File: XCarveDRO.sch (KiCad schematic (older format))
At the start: 9 parts, among them J103 USB_A, Q1 IRLML0040TR, SW103 SEL1, SW104 SEL2, U101 Teensy4.1

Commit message: Based on feedback, update silkscreen on DP101 and link to OSHPark, R201 from 10K to 1K.
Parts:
- J103: symbol Connector:USB_A -> XCarveDRO-rescue:USB_A-Connector
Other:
- note added: "DP101 Can be ordered from OshPark:\nhttps://oshpark.com/shared_projects/ZNeN5t92\nThis breakout includes R101 and Q1 so they\ncan be ignored in this schematic."
- note removed: "DP101 Can be ordered from OshPark:\nhttps://oshpark.com/shared_projects/djFs49lT"
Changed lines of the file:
@@
 	3950 850  8100 850
 $Comp
-L Connector:USB_A J103
+L XCarveDRO-rescue:USB_A-Connector J103
 U 1 1 5FADCB7A
 P 3800 5800
@@
 Wire Notes Line
 	11100 5350 6950 5350
-Text Notes 700  900  0    79   ~ 0
-DP101 Can be ordered from OshPark:\nhttps://oshpark.com/shared_projects/djFs49lT
+Text Notes 650  1100 0    79   ~ 0
+DP101 Can be ordered from OshPark:\nhttps://oshpark.com/shared_projects/ZNeN5t92\nThis breakout includes R101 and Q1 so they\ncan be ignored in this schematic.
 Wire Notes Line
-	650  600  650  1000
+	650  1100 3600 1100
 Wire Notes Line
-	650  1000 3600 1000
+	3600 600  3600 1100
 Wire Notes Line
-	3600 1000 3600 600
+	650  600  650  1100
 Wire Notes Line
-	3600 600  650  600
+	650  600  3600 600
 $EndSCHEMATC

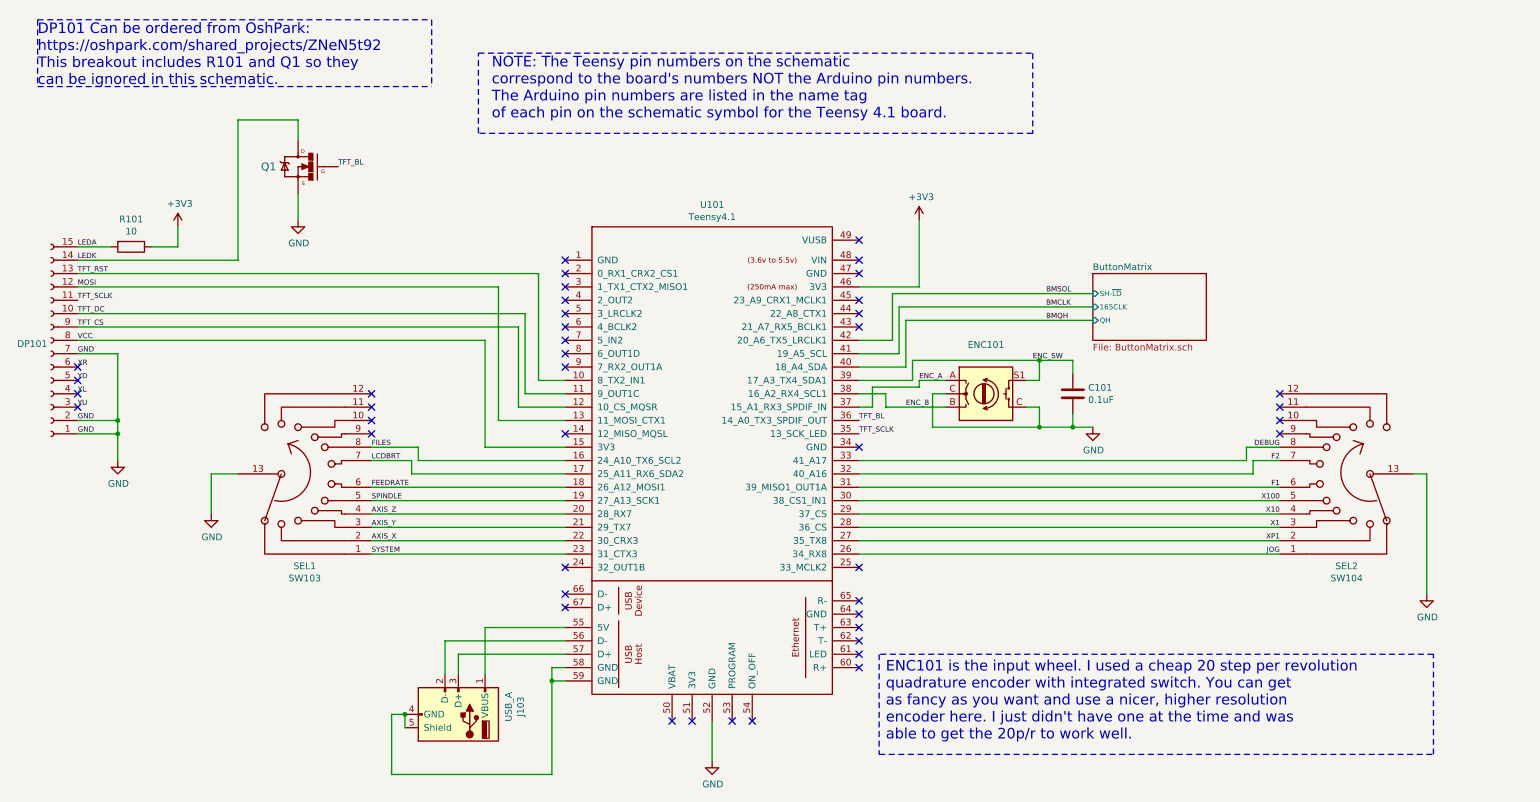
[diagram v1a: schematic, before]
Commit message: Update schematic to use the oshpark board layout so there is more consistency between the two. Update notes descriptions and bump to revision 1.
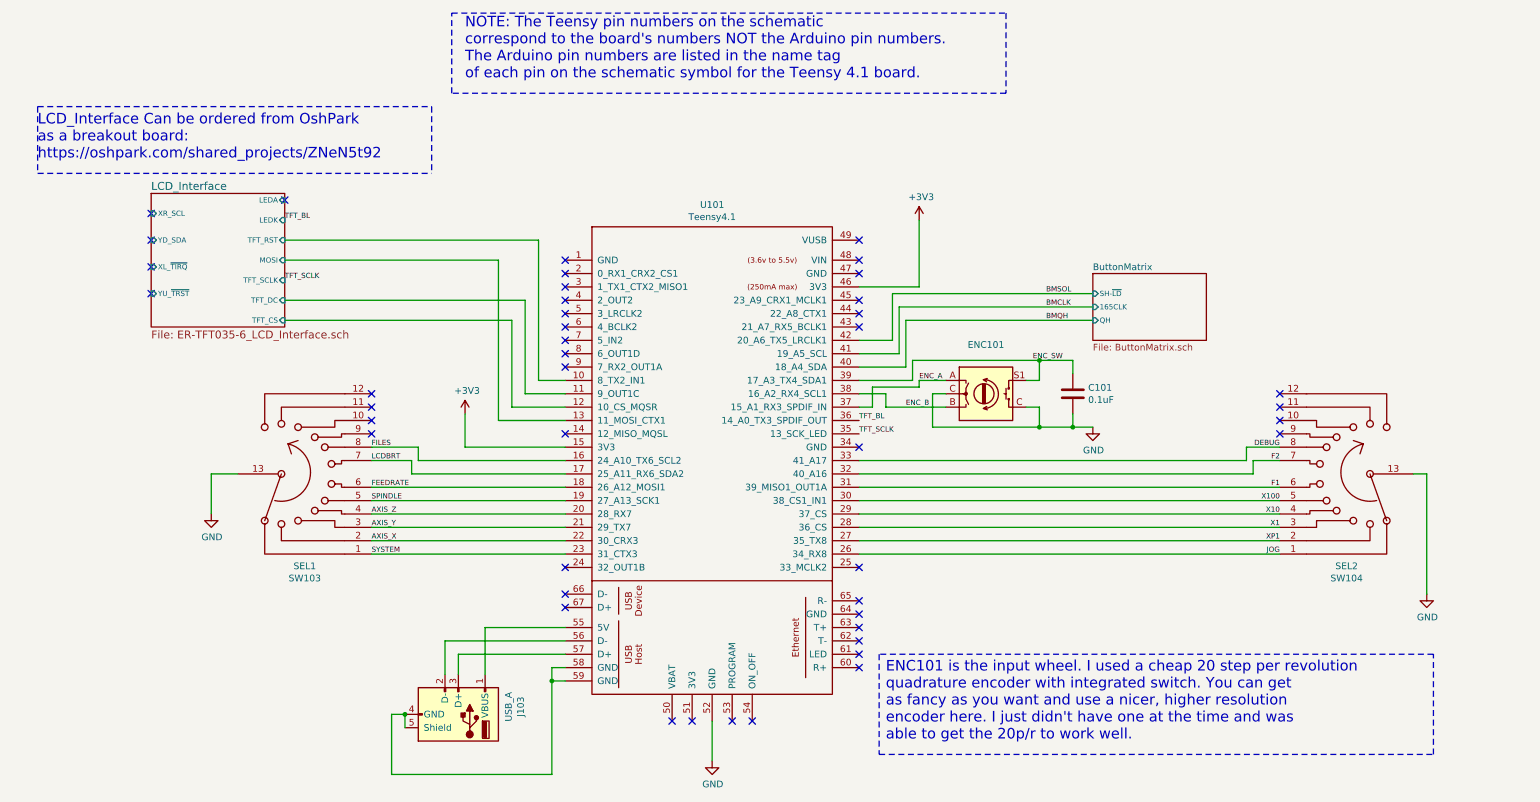
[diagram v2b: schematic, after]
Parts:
- removed DP101: Conn_01x15_Female, MarcoK:BUY_LCD_TFT035-6_320x480-BO, symbol Connector:Conn_01x15_Female
- removed Q1: IRLML0040TR, symbol MarcoK:IRLML0040TR
- removed R101: 10, symbol Device:R
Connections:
- net VCC is gone; now on net +3V3: U101.15 (3V3)
- net MOSI renamed LCD_Interface/MOSI
- net TFT_CS renamed LCD_Interface/TFT_CS
- net TFT_DC renamed LCD_Interface/TFT_DC
- net TFT_RST renamed LCD_Interface/TFT_RST
- no-connect marks 43 -> 44
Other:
- note added: "LCD_Interface Can be ordered from OshPark\nas a breakout board:\nhttps://oshpark.com/shared_projects/ZNeN5t92"
- note removed: "DP101 Can be ordered from OshPark:\nhttps://oshpark.com/shared_projects/ZNeN5t92\nThis breakout includes R101 and Q1 so they\ncan be ignored in this schematic."
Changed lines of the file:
@@
 $Descr A4 11693 8268
 encoding utf-8
-Sheet 1 2
+Sheet 1 3
 Title "GRBL Controller"
-Date "2021-01-09"
-Rev "0"
+Date "2022-01-10"
+Rev "1"
 Comp ""
-Comment1 "DP101 is a TFT LCD breakout adapter for the ER-TFT035-6 from BuyDisplay.com"
+Comment1 "MCU, encoder and selector switches."
 Comment2 ""
 Comment3 ""
@@
 	1    7750 3400
 	1    0    0    -1
-$EndComp
-Text Label 950  3600 0    39   ~ 0
-GND
-Text Label 950  3700 0    39   ~ 0
-GND
-Text Label 950  3100 0    39   ~ 0
-GND
-Text Label 950  2800 0    39   ~ 0
-TFT_DC
-Text Label 950  2600 0    39   ~ 0
-MOSI
-Text Label 950  2700 0    39   ~ 0
-TFT_SCLK
-Text Label 950  2900 0    39   ~ 0
-TFT_CS
-Text Label 950  2400 0    39   ~ 0
-LEDK
-Text Label 950  2300 0    39   ~ 0
-LEDA
-Text Label 950  3300 0    39   ~ 0
-YD
-Text Label 950  3500 0    39   ~ 0
-YU
-Text Label 950  3200 0    39   ~ 0
-XR
-Text Label 950  3400 0    39   ~ 0
-XL
-Text Label 950  2500 0    39   ~ 0
-TFT_RST
-Text Label 950  3000 0    39   ~ 0
-VCC
-$Comp
-L Connector:Conn_01x15_Female J?
-U 1 1 5FBD7E6A
-P 750 3000
-AR Path="/5FBAC065/5FBD7E6A" Ref="J?"  Part="1"
-AR Path="/5FBD7E6A" Ref="DP101"  Part="1"
-F 0 "DP101" H 778 3026 50  0000 L CNN
-F 1 "Conn_01x15_Female" H 778 2935 50  0001 L CNN
-F 2 "MarcoK:BUY_LCD_TFT035-6_320x480-BO" H 750 3000 50  0001 C CNN
-F 3 "~" H 750 3000 50  0001 C CNN
-F 4 "https://oshpark.com/shared_projects/djFs49lT" H 750 3000 50  0001 C CNN "OshPArk"
-	1    750  3000
-	-1   0    0    1
 $EndComp
 $Sheet
@@
 NoConn ~ 4600 2400
 NoConn ~ 5550 5850
-$Comp
-L power:GND #PWR0105
-U 1 1 60629CFA
-P 1250 3900
-F 0 "#PWR0105" H 1250 3650 50  0001 C CNN
-F 1 "GND" H 1255 3727 50  0000 C CNN
-F 2 "" H 1250 3900 50  0001 C CNN
-F 3 "" H 1250 3900 50  0001 C CNN
-	1    1250 3900
-	1    0    0    -1
-$EndComp
-$Comp
-L MarcoK:IRLML0040TR Q1
-U 1 1 6062DC4C
-P 2600 1700
-F 0 "Q1" H 2763 1700 59  0000 L CNN
-F 1 "IRLML0040TR" H 2763 1648 59  0001 L CNN
-F 2 "" H 2600 1700 10  0001 C CNN
-F 3 "" H 2600 1700 10  0001 C CNN
-	1    2600 1700
-	-1   0    0    -1
-$EndComp
-$Comp
-L power:GND #PWR0106
-U 1 1 6063E03D
-P 2600 2100
-F 0 "#PWR0106" H 2600 1850 50  0001 C CNN
-F 1 "GND" H 2605 1927 50  0000 C CNN
-F 2 "" H 2600 2100 50  0001 C CNN
-F 3 "" H 2600 2100 50  0001 C CNN
-	1    2600 2100
-	1    0    0    -1
-$EndComp
-$Comp
-L Device:R R101
-U 1 1 6063E605
-P 1350 2300
-F 0 "R101" V 1143 2300 50  0000 C CNN
-F 1 "10" V 1234 2300 50  0000 C CNN
-F 2 "" V 1280 2300 50  0001 C CNN
-F 3 "~" H 1350 2300 50  0001 C CNN
-	1    1350 2300
-	0    1    1    0
-$EndComp
-Wire Wire Line
-	950  2300 1200 2300
-Text Label 2900 1700 0    39   ~ 0
-TFT_BL
-Wire Wire Line
-	950  3700 1250 3700
-Wire Wire Line
-	1250 3700 1250 3900
-Wire Wire Line
-	950  3600 1250 3600
-Wire Wire Line
-	1250 3600 1250 3700
-Connection ~ 1250 3700
-NoConn ~ 950  3500
-NoConn ~ 950  3400
-NoConn ~ 950  3300
-NoConn ~ 950  3200
-Wire Wire Line
-	950  3100 1250 3100
-Wire Wire Line
-	1250 3100 1250 3600
-Connection ~ 1250 3600
-Wire Wire Line
-	950  2500 4400 2500
-Wire Wire Line
-	4400 2500 4400 3300
 Wire Wire Line
 	4400 3300 4600 3300
 Wire Wire Line
 	4600 3400 4300 3400
-Wire Wire Line
-	4300 3400 4300 2800
-Wire Wire Line
-	4300 2800 950  2800
-Wire Wire Line
-	4600 3500 4250 3500
-Wire Wire Line
-	4250 3500 4250 2900
-Wire Wire Line
-	4250 2900 950  2900
-Wire Wire Line
-	4100 2600 4100 3600
 Wire Wire Line
 	4100 3600 4600 3600
@@
 L power:+3V3 #PWR0107
 U 1 1 606A3138
-P 7250 2100
-F 0 "#PWR0107" H 7250 1950 50  0001 C CNN
-F 1 "+3V3" H 7265 2273 50  0000 C CNN
-F 2 "" H 7250 2100 50  0001 C CNN
-F 3 "" H 7250 2100 50  0001 C CNN
-	1    7250 2100
+P 3850 3550
+F 0 "#PWR0107" H 3850 3400 50  0001 C CNN
+F 1 "+3V3" H 3865 3723 50  0000 C CNN
+F 2 "" H 3850 3550 50  0001 C CNN
+F 3 "" H 3850 3550 50  0001 C CNN
+	1    3850 3550
 	1    0    0    -1
 $EndComp
@@
 	7250 2600 7250 2100
 NoConn ~ 6800 2500
-$Comp
-L power:+3V3 #PWR0108
-U 1 1 606AB99C
-P 1700 2150
-F 0 "#PWR0108" H 1700 2000 50  0001 C CNN
-F 1 "+3V3" H 1715 2323 50  0000 C CNN
-F 2 "" H 1700 2150 50  0001 C CNN
-F 3 "" H 1700 2150 50  0001 C CNN
-	1    1700 2150
-	1    0    0    -1
-$EndComp
-Wire Wire Line
-	1500 2300 1700 2300
-Wire Wire Line
-	1700 2300 1700 2150
-Wire Wire Line
-	4000 3800 4000 3000
-Wire Wire Line
-	4000 3000 950  3000
-Wire Wire Line
-	4000 3800 4600 3800
-Wire Wire Line
-	950  2600 4100 2600
-Wire Wire Line
-	2600 2100 2600 1900
-Wire Wire Line
-	950  2400 2150 2400
-Wire Wire Line
-	2150 2400 2150 1350
-Wire Wire Line
-	2150 1350 2600 1350
-Wire Wire Line
-	2600 1350 2600 1500
 Text Label 7250 3300 0    39   ~ 0
 ENC_A
@@
 Text Label 8200 2850 0    39   ~ 0
 BMQH
-Text Notes 4050 1350 0    79   ~ 0
+Text Notes 3850 1050 0    79   ~ 0
 NOTE: The Teensy pin numbers on the schematic\ncorrespond to the board's numbers NOT the Arduino pin numbers.\nThe Arduino pin numbers are listed in the name tag\nof each pin on the schematic symbol for the Teensy 4.1 board.
 Wire Notes Line
-	8100 850  8100 1450
-Wire Notes Line
-	8100 1450 3950 1450
-Wire Notes Line
-	3950 1450 3950 850
-Wire Notes Line
-	3950 850  8100 850
+	7900 550  7900 1150
+Wire Notes Line
+	7900 1150 3750 1150
+Wire Notes Line
+	3750 1150 3750 550
+Wire Notes Line
+	3750 550  7900 550
 $Comp
 L XCarveDRO-rescue:USB_A-Connector J103
@@
 Wire Notes Line
 	11100 5350 6950 5350
-Text Notes 650  1100 0    79   ~ 0
-DP101 Can be ordered from OshPark:\nhttps://oshpark.com/shared_projects/ZNeN5t92\nThis breakout includes R101 and Q1 so they\ncan be ignored in this schematic.
-Wire Notes Line
-	650  1100 3600 1100
-Wire Notes Line
-	3600 600  3600 1100
-Wire Notes Line
-	650  600  650  1100
-Wire Notes Line
-	650  600  3600 600
+$Sheet
+S 1500 1900 1000 1000
+U 61DD28D7
+F0 "LCD_Interface" 59
+F1 "ER-TFT035-6_LCD_Interface.sch" 59
+F2 "LEDA" I R 2500 1950 39
+F3 "LEDK" I R 2500 2100 39
+F4 "TFT_RST" I R 2500 2250 39
+F5 "MOSI" I R 2500 2400 39
+F6 "TFT_SCLK" I R 2500 2550 39
+F7 "TFT_DC" I R 2500 2700 39
+F8 "TFT_CS" I R 2500 2850 39
+F9 "XR_SCL" I L 1500 2050 39
+F10 "YD_SDA" I L 1500 2250 39
+F11 "XL_~TIRQ" I L 1500 2450 39
+F12 "YU_~TRST" I L 1500 2650 39
+$EndSheet
+NoConn ~ 1500 2050
+NoConn ~ 1500 2250
+NoConn ~ 1500 2450
+NoConn ~ 1500 2650
+NoConn ~ 2500 1950
+Text Label 2500 2100 0    39   ~ 0
+TFT_BL
+Text Label 2500 2550 0    39   ~ 0
+TFT_SCLK
+Wire Wire Line
+	2500 2250 4400 2250
+Wire Wire Line
+	4400 2250 4400 3300
+Wire Wire Line
+	2500 2400 4100 2400
+Wire Wire Line
+	4100 2400 4100 3600
+Wire Wire Line
+	2500 2700 4300 2700
+Wire Wire Line
+	4300 2700 4300 3400
+Wire Wire Line
+	2500 2850 4200 2850
+Wire Wire Line
+	4200 2850 4200 3500
+Wire Wire Line
+	4200 3500 4600 3500
+Wire Wire Line
+	3850 3550 3850 3800
+Wire Wire Line
+	3850 3800 4600 3800
+$Comp
+L power:+3V3 #PWR?
+U 1 1 61F3878F
+P 7250 2100
+F 0 "#PWR?" H 7250 1950 50  0001 C CNN
+F 1 "+3V3" H 7265 2273 50  0000 C CNN
+F 2 "" H 7250 2100 50  0001 C CNN
+F 3 "" H 7250 2100 50  0001 C CNN
+	1    7250 2100
+	1    0    0    -1
+$EndComp
+Wire Notes Line
+	650  1250 3600 1250
+Wire Notes Line
+	650  1250 650  1750
+Wire Notes Line
+	3600 1250 3600 1750
+Wire Notes Line
+	650  1750 3600 1750
+Text Notes 650  1650 0    79   ~ 0
+LCD_Interface Can be ordered from OshPark\nas a breakout board:\nhttps://oshpark.com/shared_projects/ZNeN5t92
 $EndSCHEMATC
